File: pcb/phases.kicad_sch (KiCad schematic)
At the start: 51 parts, among them J13 Phase_Bitshifter, J14 Phase_Button_Decoder, SW18 Reset, SW19 +1, SW20 +10, SW21 -10, SW22 -1, SW23 x2, SW24 /2, SW25 Random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

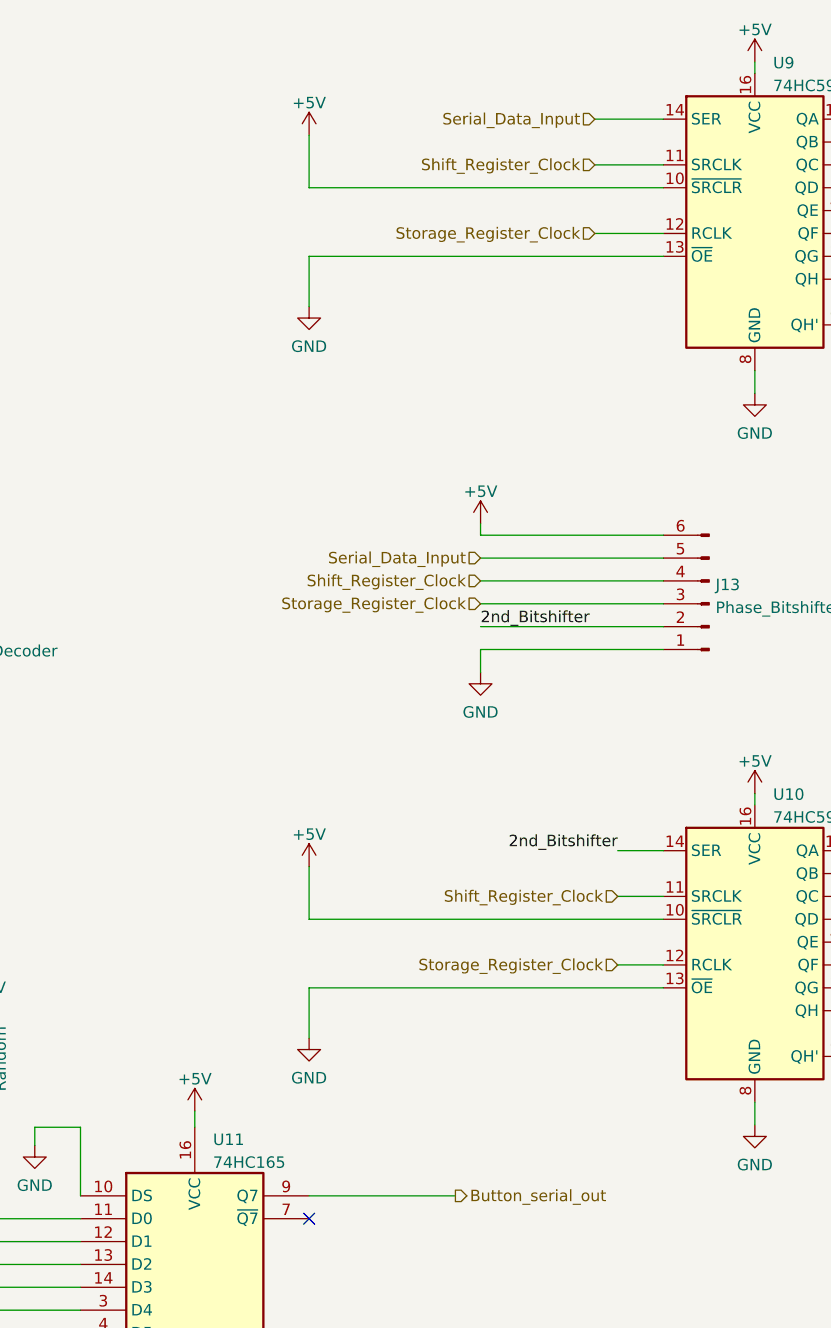
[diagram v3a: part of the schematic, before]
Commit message: pulldown to signals
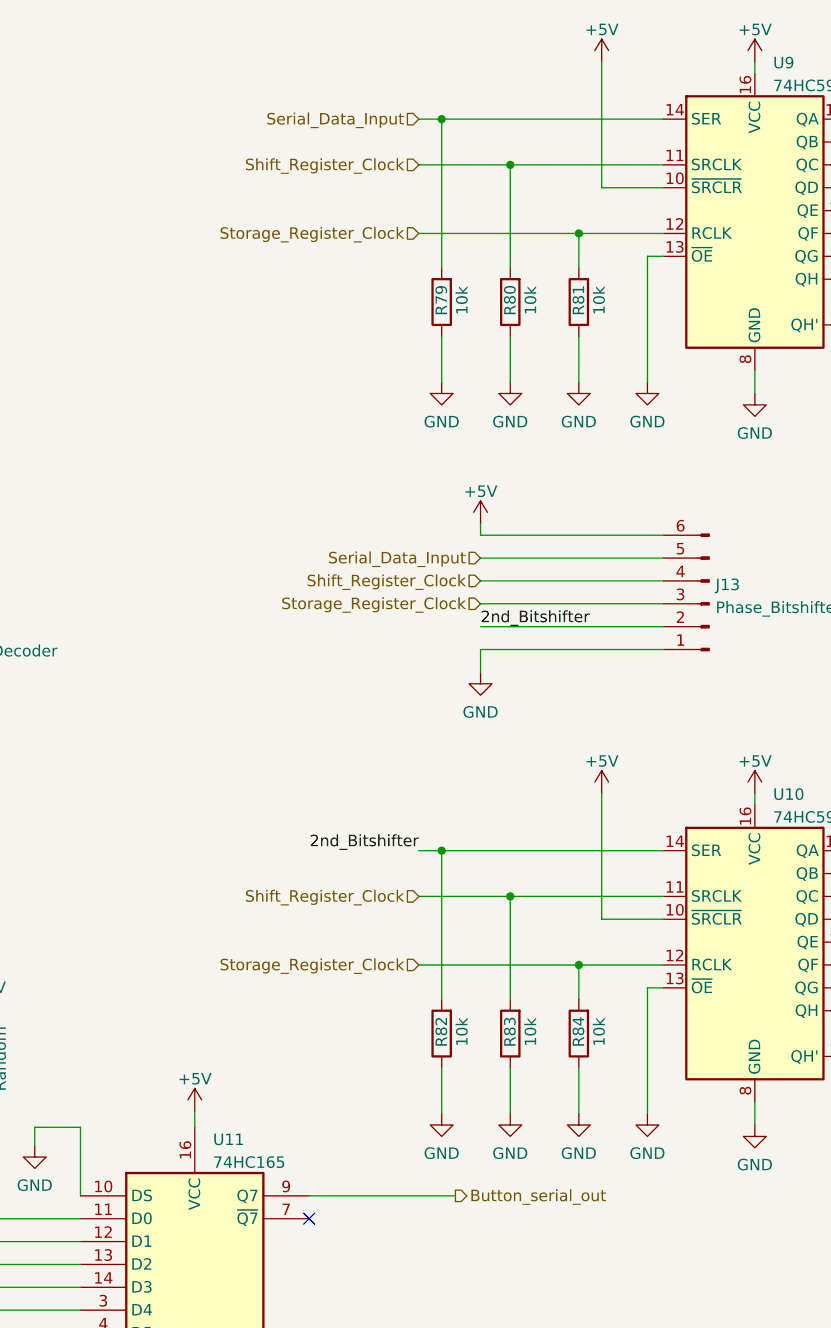
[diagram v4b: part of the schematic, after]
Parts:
- added R79, R80, R81, R82, R83, R84: 10k, Resistor_THT:R_Axial_DIN0207_L6.3mm_D2.5mm_P10.16mm_Horizontal, symbol Device:R
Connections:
- net 2nd_Bitshifter: now also R82.2
- net GND: now also R79.1, R80.1, R81.1, R82.1, R83.1, R84.1
- net Serial_Data_Input: now also R79.2
- net Shift_Register_Clock: now also R80.2, R83.2
- net Storage_Register_Clock: now also R81.2, R84.2
